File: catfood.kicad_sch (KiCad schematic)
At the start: 0 parts

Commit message: NAND
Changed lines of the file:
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@@
-    (effects (font (size 1.27 1.27)) (justify left bottom))
-  )
-  (text "TODO" (at 146.05 66.04 0)
     (effects (font (size 1.27 1.27)) (justify left bottom))
   )
@@
       (reference "#PWR?") (unit 1) (value "GND") (footprint "")
     )
+    (path "/070bf4c0-20e4-46ea-85ff-83bf5a0585a3/360fbb00-eab2-4c3a-bed8-73e62be0b014"
+      (reference "#PWR?") (unit 1) (value "GND") (footprint "")
+    )
     (path "/2ab15384-2aea-4732-9049-deba0d18aefc/36ed9b09-6eb4-4839-be08-ac8eece96bec"
       (reference "#PWR?") (unit 1) (value "GND") (footprint "")
@@
       (reference "#PWR?") (unit 1) (value "GND") (footprint "")
     )
+    (path "/070bf4c0-20e4-46ea-85ff-83bf5a0585a3/4ca9f10e-da94-4d2d-8d2a-3d6b0d56b421"
+      (reference "#PWR?") (unit 1) (value "GND") (footprint "")
+    )
     (path "/f3ebd76f-b12f-4b33-bd17-edae6bffa200/4cdf8f5c-deb2-4d44-8035-cb7521c0c8fc"
       (reference "#PWR?") (unit 1) (value "GND") (footprint "")
@@
     )
     (path "/798b3f66-4b87-46ea-bb18-dc03ff32d68c/4da48c9e-dee9-4f0d-9648-5b0bef819dcf"
+      (reference "#PWR?") (unit 1) (value "GND") (footprint "")
+    )
+    (path "/070bf4c0-20e4-46ea-85ff-83bf5a0585a3/4dbfb975-416f-446a-b052-db5a4f7aa209"
       (reference "#PWR?") (unit 1) (value "GND") (footprint "")
     )
@@
       (reference "#PWR?") (unit 1) (value "VDD_3V3_IN") (footprint "")
     )
+    (path "/070bf4c0-20e4-46ea-85ff-83bf5a0585a3/5f4ac017-74ad-4dbf-8c86-47c1914a17ee"
+      (reference "#PWR?") (unit 1) (value "VDD_3V3") (footprint "")
+    )
     (path "/2ab15384-2aea-4732-9049-deba0d18aefc/61503b57-566d-401b-8de6-a1b10e7ab9c8"
       (reference "#PWR?") (unit 1) (value "GND") (footprint "")
@@
       (reference "#PWR?") (unit 1) (value "GND") (footprint "")
     )
+    (path "/070bf4c0-20e4-46ea-85ff-83bf5a0585a3/b8133473-cb4c-4e44-96c3-ddac821db66a"
+      (reference "#PWR?") (unit 1) (value "VDD_3V3") (footprint "")
+    )
     (path "/e1490e46-0057-4bf0-bc0e-723ccd3e21a2/b827c2ad-59bd-4ef9-9a5d-f59e81cd4026"
       (reference "#PWR?") (unit 1) (value "VDD_3V3") (footprint "")
@@
       (reference "#PWR?") (unit 1) (value "GND") (footprint "")
     )
+    (path "/070bf4c0-20e4-46ea-85ff-83bf5a0585a3/d63a2943-19af-43bd-8687-dd9b49001b4d"
+      (reference "#PWR?") (unit 1) (value "VDD_3V3") (footprint "")
+    )
     (path "/f3ebd76f-b12f-4b33-bd17-edae6bffa200/dcfe82b4-728e-47e9-b293-74162304364f"
       (reference "#PWR?") (unit 1) (value "GND") (footprint "")
@@
     )
     (path "/e1490e46-0057-4bf0-bc0e-723ccd3e21a2/e31ef5d6-c132-4f81-adff-ead0c967154e"
+      (reference "#PWR?") (unit 1) (value "GND") (footprint "")
+    )
+    (path "/070bf4c0-20e4-46ea-85ff-83bf5a0585a3/e66d1236-6d6a-4de8-8bd1-3f02519a4590"
       (reference "#PWR?") (unit 1) (value "GND") (footprint "")
     )
@@
       (reference "C?") (unit 1) (value "0.1uF 0402") (footprint "")
     )
+    (path "/070bf4c0-20e4-46ea-85ff-83bf5a0585a3/1b6fdecb-8a58-4c5a-95f3-3856ea0462b8"
+      (reference "C?") (unit 1) (value "18pF 0402") (footprint "")
+    )
     (path "/2ab15384-2aea-4732-9049-deba0d18aefc/1c52b611-d7b1-439a-a97e-83e2327b01ad"
       (reference "C?") (unit 1) (value "0.22uF 0402") (footprint "")
@@
       (reference "C?") (unit 1) (value "4.7uF 0603") (footprint "")
     )
+    (path "/070bf4c0-20e4-46ea-85ff-83bf5a0585a3/24391822-3b40-4163-a59d-bc95bf4eef05"
+      (reference "C?") (unit 1) (value "0.1uF 0402") (footprint "")
+    )
     (path "/2ab15384-2aea-4732-9049-deba0d18aefc/29e69fb6-e5c4-4402-94ce-1d25ecfe709d"
       (reference "C?") (unit 1) (value "0.22uF 0402") (footprint "")
@@
       (reference "C?") (unit 1) (value "2.2pF 0402") (footprint "")
     )
+    (path "/070bf4c0-20e4-46ea-85ff-83bf5a0585a3/383e4298-f3b5-4382-924b-c02dcdcada54"
+      (reference "C?") (unit 1) (value "0.22uF 0402") (footprint "")
+    )
     (path "/a3321ecb-7e45-4b88-8ac6-91bd0372968a/395f1d08-680b-46b5-9161-f51700aa46c8"
       (reference "C?") (unit 1) (value "4.7uF 0603") (footprint "")
@@
       (reference "C?") (unit 1) (value "0.001uF 2kV") (footprint "")
     )
+    (path "/070bf4c0-20e4-46ea-85ff-83bf5a0585a3/3c6a553a-1402-408b-880a-a780852f3a6e"
+      (reference "C?") (unit 1) (value "0.1uF 0402") (footprint "")
+    )
     (path "/a3321ecb-7e45-4b88-8ac6-91bd0372968a/438e023e-96ba-4c04-a106-f38aec48996d"
       (reference "C?") (unit 1) (value "0.1uF 0402") (footprint "")
@@
     (path "/a3321ecb-7e45-4b88-8ac6-91bd0372968a/4e30a38f-4b0d-4b1e-83d1-e3b4469b28de"
       (reference "C?") (unit 1) (value "0.1uF 0402") (footprint "")
+    )
+    (path "/070bf4c0-20e4-46ea-85ff-83bf5a0585a3/4e7d2c3a-0960-47aa-a60d-a4772f760e53"
+      (reference "C?") (unit 1) (value "4.7uF 0603") (footprint "")
     )
     (path "/798b3f66-4b87-46ea-bb18-dc03ff32d68c/4f846b06-0935-45d1-93d3-fe7ec224f174"
@@
       (reference "C?") (unit 1) (value "0.1uF 0402") (footprint "")
     )
+    (path "/070bf4c0-20e4-46ea-85ff-83bf5a0585a3/7a6e2141-7807-4e00-b557-c6dd3e8fe14c"
+      (reference "C?") (unit 1) (value "0.1uF 0402") (footprint "")
+    )
     (path "/2ab15384-2aea-4732-9049-deba0d18aefc/7eae51e9-c0a8-494a-ace8-937c6ec4e35f"
       (reference "C?") (unit 1) (value "0.22uF 0402") (footprint "")
@@
       (reference "C?") (unit 1) (value "0.1uF 0402") (footprint "")
     )
+    (path "/070bf4c0-20e4-46ea-85ff-83bf5a0585a3/b44a1c52-654a-41b9-8545-3b7fc20cf3bb"
+      (reference "C?") (unit 1) (value "0.1uF 0402") (footprint "")
+    )
     (path "/e1490e46-0057-4bf0-bc0e-723ccd3e21a2/bc935aa3-fd29-4f19-8ec2-0039b88ff28c"
       (reference "C?") (unit 1) (value "10uF 0805") (footprint "")
@@
       (reference "R?") (unit 1) (value "1.5k 0402") (footprint "")
     )
+    (path "/070bf4c0-20e4-46ea-85ff-83bf5a0585a3/3fa70e6d-967c-4971-8339-e34f2dad6880"
+      (reference "R?") (unit 1) (value "10k 0402") (footprint "")
+    )
     (path "/a3321ecb-7e45-4b88-8ac6-91bd0372968a/4ed8581b-9f1f-4a89-ab79-6106c3990865"
       (reference "R?") (unit 1) (value "75R 0402") (footprint "")
@@
       (reference "R?") (unit 1) (value "75R 0402") (footprint "")
     )
+    (path "/070bf4c0-20e4-46ea-85ff-83bf5a0585a3/5d4e1476-8372-44c6-8c9e-16cbab6dd0e5"
+      (reference "R?") (unit 1) (value "10R 0402") (footprint "")
+    )
     (path "/798b3f66-4b87-46ea-bb18-dc03ff32d68c/5d93b82d-60c9-4f39-a356-acf86c9cfd11"
       (reference "R?") (unit 1) (value "1.5k 0402 1%") (footprint "")
@@
       (reference "R?") (unit 1) (value "330R 0402") (footprint "")
     )
+    (path "/070bf4c0-20e4-46ea-85ff-83bf5a0585a3/62f6b269-4cab-48c5-8d1a-8dd0a55ae976"
+      (reference "R?") (unit 1) (value "10R 0402") (footprint "")
+    )
     (path "/798b3f66-4b87-46ea-bb18-dc03ff32d68c/65379736-38fe-4559-a56d-5aa06e3b6aae"
       (reference "R?") (unit 1) (value "10k 0402") (footprint "")
@@
       (reference "R?") (unit 1) (value "75R 0402") (footprint "")
     )
+    (path "/070bf4c0-20e4-46ea-85ff-83bf5a0585a3/c5217b02-ab8d-4859-865a-bea3d62c8612"
+      (reference "R?") (unit 1) (value "10k 0402") (footprint "")
+    )
     (path "/a3321ecb-7e45-4b88-8ac6-91bd0372968a/ca0ca9c1-e927-4098-a771-d23f5f35d208"
       (reference "R?") (unit 1) (value "10R 0402") (footprint "")
@@
       (reference "R?") (unit 1) (value "75R 0402") (footprint "")
     )
+    (path "/070bf4c0-20e4-46ea-85ff-83bf5a0585a3/cf3e865c-56a6-4e5c-8998-0d52854bd666"
+      (reference "R?") (unit 1) (value "0R 0402") (footprint "")
+    )
     (path "/798b3f66-4b87-46ea-bb18-dc03ff32d68c/d2109bc3-90ca-4fc9-ac31-a2095979d398"

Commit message: USB, GPIO
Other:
- sheet GPIO ports: added ENET_MDC, ENET_MDIO, ~{ENET1_RST}; removed none
- note added: "TODO: onoff/PoR/pmic_on_req test points LED Ethernet TVS (Rclamp3374N) USB: check: host port capacitance USB_OTG2 separate vbus: current limit / load switch"
- note removed: "TODO: onoff/PoR/pmic_on_req test points"

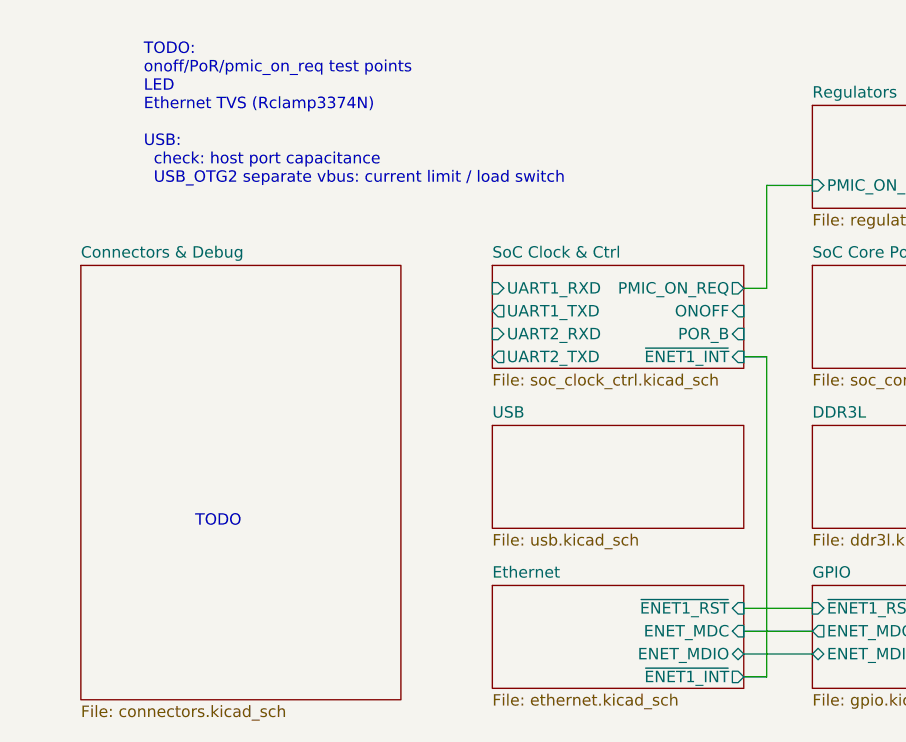
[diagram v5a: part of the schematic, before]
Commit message: USB host port capacitance, load switch
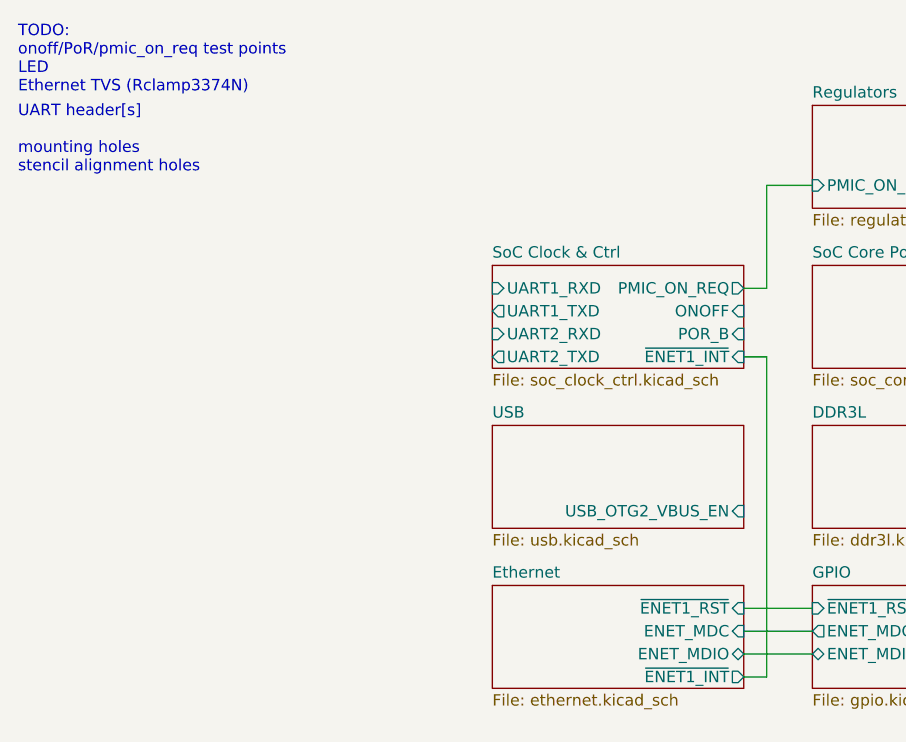
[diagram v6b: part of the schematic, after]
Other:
- removed sheet Connectors & Debug
- sheet USB ports: added USB_OTG2_VBUS_EN; removed none
- note added: "TODO: onoff/PoR/pmic_on_req test points LED Ethernet TVS (Rclamp3374N)"
- note added: "UART header[s] mounting holes stencil alignment holes"
- note removed: "TODO"
- note removed: "TODO: onoff/PoR/pmic_on_req test points LED Ethernet TVS (Rclamp3374N) USB: check: host port capacitance USB_OTG2 separate vbus: current limit / load switch"
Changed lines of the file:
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@@
     (stroke (width 0) (type default) (color 0 0 0 0))
   )
-  (text "TODO" (at 34.29 71.12 0)
+  (text "UART header[s]\n\nmounting holes\nstencil alignment holes"
+    (at 14.605 31.75 0)
     (effects (font (size 1.27 1.27)) (justify left bottom))
   )
-  (text "TODO:\nonoff/PoR/pmic_on_req test points\nLED\nEthernet TVS (Rclamp3374N)\n\nUSB:\n  check: host port capacitance\n  USB_OTG2 separate vbus: current limit / load switch"
-    (at 28.575 33.02 0)
+  (text "TODO:\nonoff/PoR/pmic_on_req test points\nLED\nEthernet TVS (Rclamp3374N)"
+    (at 14.605 22.86 0)
     (effects (font (size 1.27 1.27)) (justify left bottom))
   )
@@
       (effects (font (size 1.27 1.27)) (justify left top))
     )
-  )
-  (sheet (at 21.59 41.91) (size 35.56 48.26) (fields_autoplaced)
-    (stroke (width 0.1524) (type solid) (color 0 0 0 0))
-    (fill (color 0 0 0 0.0000))
-    (property "Sheet name" "Connectors & Debug" (id 0) (at 21.59 41.1984 0)
-      (effects (font (size 1.27 1.27)) (justify left bottom))
-    )
-    (property "Sheet file" "connectors.kicad_sch" (id 1) (at 21.59 90.7546 0)
-      (effects (font (size 1.27 1.27)) (justify left top))
+    (pin "USB_OTG2_VBUS_EN" input (at 95.25 69.215 0)
+      (effects (font (size 1.27 1.27)) (justify right))
     )
   )
@@
     (path "/a3321ecb-7e45-4b88-8ac6-91bd0372968a" (page "7"))
     (path "/1f7c86fd-838a-4fbd-9ad6-fe73640b467f" (page "9"))
-    (path "/9e9d365b-50b6-4e60-9e2a-c60cbf357141" (page "10"))
     (path "/f3ebd76f-b12f-4b33-bd17-edae6bffa200" (page "11"))
   )
@@
       (reference "#PWR?") (unit 1) (value "VDD_3V3") (footprint "")
     )
-    (path "/8268d581-e104-4459-841c-45d3bd21be9e/341db799-e758-4e15-9577-e43b7a9c5738"
-      (reference "#PWR?") (unit 1) (value "VDD_5V") (footprint "")
-    )
     (path "/a3321ecb-7e45-4b88-8ac6-91bd0372968a/345a5b3f-89e0-4b1b-b676-e4db7da5dd11"
       (reference "#PWR?") (unit 1) (value "GND") (footprint "")
@@
       (reference "#PWR?") (unit 1) (value "GND") (footprint "")
     )
-    (path "/8268d581-e104-4459-841c-45d3bd21be9e/4f2f49e6-15ac-449d-81c9-99d6c40745d2"
-      (reference "#PWR?") (unit 1) (value "VDD_5V") (footprint "")
+    (path "/8268d581-e104-4459-841c-45d3bd21be9e/50c68f57-f86f-431e-b695-351a3335ed26"
+      (reference "#PWR?") (unit 1) (value "GND") (footprint "")
     )
     (path "/2ab15384-2aea-4732-9049-deba0d18aefc/517f4559-6c18-42bc-ace7-9e6e9aca8927"
@@
       (reference "#PWR?") (unit 1) (value "GND") (footprint "")
     )
+    (path "/8268d581-e104-4459-841c-45d3bd21be9e/b6c5bfc4-0b45-48f9-8c24-012c0550ab0b"
+      (reference "#PWR?") (unit 1) (value "GND") (footprint "")
+    )
     (path "/1f7c86fd-838a-4fbd-9ad6-fe73640b467f/b7a03d78-998f-472d-bc64-c75994d0fddd"
       (reference "#PWR?") (unit 1) (value "VDD_3V3") (footprint "")
@@
       (reference "#PWR?") (unit 1) (value "VDD_3V3") (footprint "")
     )
+    (path "/8268d581-e104-4459-841c-45d3bd21be9e/db3d0114-48c5-4602-a698-cff902091733"
+      (reference "#PWR?") (unit 1) (value "GND") (footprint "")
+    )
     (path "/f3ebd76f-b12f-4b33-bd17-edae6bffa200/dcfe82b4-728e-47e9-b293-74162304364f"
       (reference "#PWR?") (unit 1) (value "GND") (footprint "")
@@
     )
     (path "/070bf4c0-20e4-46ea-85ff-83bf5a0585a3/e66d1236-6d6a-4de8-8bd1-3f02519a4590"
+      (reference "#PWR?") (unit 1) (value "GND") (footprint "")
+    )
+    (path "/8268d581-e104-4459-841c-45d3bd21be9e/e68a833a-fcd8-42b4-8c98-defe7cd60ad5"
       (reference "#PWR?") (unit 1) (value "GND") (footprint "")
     )
@@
       (reference "#PWR?") (unit 1) (value "GND") (footprint "")
     )
+    (path "/8268d581-e104-4459-841c-45d3bd21be9e/f7f99ae5-a4ec-46f5-96fc-aea40f288814"
+      (reference "#PWR?") (unit 1) (value "VDD_5V") (footprint "")
+    )
     (path "/2ab15384-2aea-4732-9049-deba0d18aefc/f824c6a2-8fff-426d-81d1-d8d81f63e3e4"
       (reference "#PWR?") (unit 1) (value "GND") (footprint "")
@@
       (reference "C?") (unit 1) (value "0.22uF 0402") (footprint "")
     )
+    (path "/8268d581-e104-4459-841c-45d3bd21be9e/2b28acef-6446-4f9d-8527-5125b2dca488"
+      (reference "C?") (unit 1) (value "1uF 0402") (footprint "")
+    )
+    (path "/8268d581-e104-4459-841c-45d3bd21be9e/2d7c85be-3544-4863-8c60-678b913f513c"
+      (reference "C?") (unit 1) (value "10uF 0805") (footprint "")
+    )
     (path "/2ab15384-2aea-4732-9049-deba0d18aefc/2ed208a5-6fda-4953-8bec-1a42df45ee65"
       (reference "C?") (unit 1) (value "4.7uF 0603") (footprint "")
@@
       (reference "C?") (unit 1) (value "0.1uF 0402") (footprint "")
     )
+    (path "/8268d581-e104-4459-841c-45d3bd21be9e/560b3e2b-f4b5-4e60-a5df-52d0eaca357a"
+      (reference "C?") (unit 1) (value "10uF 0805") (footprint "")
+    )
     (path "/798b3f66-4b87-46ea-bb18-dc03ff32d68c/5cef9ca8-b0dc-421b-bc60-51fa2a5a759f"
       (reference "C?") (unit 1) (value "0.22uF 0402") (footprint "")
@@
       (reference "C?") (unit 1) (value "0.1uF 0402") (footprint "")
     )
+    (path "/8268d581-e104-4459-841c-45d3bd21be9e/7b61555f-3201-4817-97a0-aceac9651b47"
+      (reference "C?") (unit 1) (value "0.1uF 0402") (footprint "")
+    )
     (path "/2ab15384-2aea-4732-9049-deba0d18aefc/7eae51e9-c0a8-494a-ace8-937c6ec4e35f"
       (reference "C?") (unit 1) (value "0.22uF 0402") (footprint "")
@@
       (reference "C?") (unit 1) (value "0.22uF 0402") (footprint "")
     )
+    (path "/8268d581-e104-4459-841c-45d3bd21be9e/988f5d79-f00d-4964-a146-5287e5d95386"
+      (reference "C?") (unit 1) (value "10uF 0805") (footprint "")
+    )
+    (path "/8268d581-e104-4459-841c-45d3bd21be9e/a7bc8b0e-2578-46b6-bfa2-e919f3857342"
+      (reference "C?") (unit 1) (value "100uF 1210") (footprint "")
+    )
     (path "/f3ebd76f-b12f-4b33-bd17-edae6bffa200/a87df369-a262-4d54-8dc1-e378fe51a6a8"
       (reference "C?") (unit 1) (value "18pF 0402") (footprint "")
@@
       (reference "J?") (unit 1) (value "USB4110") (footprint "")
     )
+    (path "/8268d581-e104-4459-841c-45d3bd21be9e/270fc1a4-a113-4172-bb2d-5610c62f4150"
+      (reference "J?") (unit 1) (value "USB_A") (footprint "")
+    )
     (path "/a3321ecb-7e45-4b88-8ac6-91bd0372968a/d659948c-b9c1-468e-a825-79281db4b0f0"
       (reference "J?") (unit 1) (value "TE_1888250-1") (footprint "")
     )
-    (path "/8268d581-e104-4459-841c-45d3bd21be9e/fa961903-34b1-4d74-a500-df4bb809f2ca"
-      (reference "J?") (unit 1) (value "USB_A") (footprint "")
-    )
     (path "/f3ebd76f-b12f-4b33-bd17-edae6bffa200/d9f86fe3-faf0-49d5-b889-4315b9a9655e"
       (reference "JP?") (unit 1) (value "SolderJumper_2_Open") (footprint "")
@@
       (reference "R?") (unit 1) (value "12.4k 0402 1%") (footprint "")
     )
+    (path "/8268d581-e104-4459-841c-45d3bd21be9e/0eaa51cd-317d-4cbb-8721-ca88a9b15f3c"
+      (reference "R?") (unit 1) (value "100k 0402") (footprint "")
+    )
     (path "/a3321ecb-7e45-4b88-8ac6-91bd0372968a/10365d67-ddbf-4773-b1ab-7af1fc2025ed"
       (reference "R?") (unit 1) (value "10k 0402") (footprint "")
@@
       (reference "R?") (unit 1) (value "1.5k 0402 1%") (footprint "")
     )
+    (path "/8268d581-e104-4459-841c-45d3bd21be9e/962089dd-796d-4b94-b035-5281fd84229d"
+      (reference "R?") (unit 1) (value "6.8k 0402 1%") (footprint "")
+    )
     (path "/a3321ecb-7e45-4b88-8ac6-91bd0372968a/a50c56ad-7755-41e0-b64c-5eceff35ba7c"
       (reference "R?") (unit 1) (value "330R 0402") (footprint "")
@@
       (reference "U?") (unit 1) (value "MT29F4G08ABAEAH4") (footprint "")
     )
+    (path "/8268d581-e104-4459-841c-45d3bd21be9e/acc46387-a1a3-4c00-a32d-d1bc835050c8"
+      (reference "U?") (unit 1) (value "AP22615AWU-7") (footprint "")
+    )
     (path "/a3321ecb-7e45-4b88-8ac6-91bd0372968a/bdbfdce4-d165-490f-9bbb-5d1a15aea6a5"

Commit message: Update notes
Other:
- sheet GPIO ports: added USB_OTG2_VBUS_EN; removed none
- note added: "TODO: onoff/PoR/pmic_on_req test points LED Ethernet TVS (Rclamp3374N) UART header[s] mounting holes stencil alignment holes Consider: SDIO WiFi I2C/SPI/UART2/few GPIOs in a shrouded R/A header"
- note removed: "TODO: onoff/PoR/pmic_on_req test points LED Ethernet TVS (Rclamp3374N)"
- note removed: "UART header[s] mounting holes stencil alignment holes"
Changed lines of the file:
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@@
+    (stroke (width 0) (type default) (color 0 0 0 0))
+  )
+  (wire (pts (xy 99.06 69.215) (xy 99.06 87.63))
     (stroke (width 0) (type default) (color 0 0 0 0))
   )
   (wire (pts (xy 95.25 85.09) (xy 102.87 85.09))
+    (stroke (width 0) (type default) (color 0 0 0 0))
+  )
+  (wire (pts (xy 102.87 87.63) (xy 99.06 87.63))
     (stroke (width 0) (type default) (color 0 0 0 0))
   )
@@
     (stroke (width 0) (type default) (color 0 0 0 0))
   )
+  (wire (pts (xy 95.25 69.215) (xy 99.06 69.215))
+    (stroke (width 0) (type default) (color 0 0 0 0))
+  )
   (wire (pts (xy 97.79 87.63) (xy 95.25 87.63))
     (stroke (width 0) (type default) (color 0 0 0 0))
   )
-  (text "UART header[s]\n\nmounting holes\nstencil alignment holes"
-    (at 14.605 31.75 0)
-    (effects (font (size 1.27 1.27)) (justify left bottom))
-  )
-  (text "TODO:\nonoff/PoR/pmic_on_req test points\nLED\nEthernet TVS (Rclamp3374N)"
-    (at 14.605 22.86 0)
+  (text "TODO:\nonoff/PoR/pmic_on_req test points\nLED\nEthernet TVS (Rclamp3374N)\nUART header[s]\n\nmounting holes\nstencil alignment holes\n\nConsider:\nSDIO WiFi\nI2C/SPI/UART2/few GPIOs in a shrouded R/A header"
+    (at 13.335 37.465 0)
     (effects (font (size 1.27 1.27)) (justify left bottom))
   )
@@
       (effects (font (size 1.27 1.27)) (justify left))
     )
+    (pin "USB_OTG2_VBUS_EN" output (at 102.87 87.63 180)
+      (effects (font (size 1.27 1.27)) (justify left))
+    )
